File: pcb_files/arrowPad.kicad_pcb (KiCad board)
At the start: 2 copper layers, 43 parts, among them J1 AudioJack3_Ground, J2 AudioJack3_Ground, K1 KEYSW, K10 KEYSW, K11 KEYSW, K12 KEYSW, K13 KEYSW, K14 KEYSW, K15 KEYSW, K16 KEYSW, K2 KEYSW, K3 KEYSW, K4 KEYSW, K5 KEYSW, K6 KEYSW, K7 KEYSW, K8 KEYSW, K9 KEYSW, U1 ProMicro, U2 NRF24L01_Breakout, U3 ADG417BN, U4 AMS1117-3.3, U5 ADG417BN, U6 ADG417BN

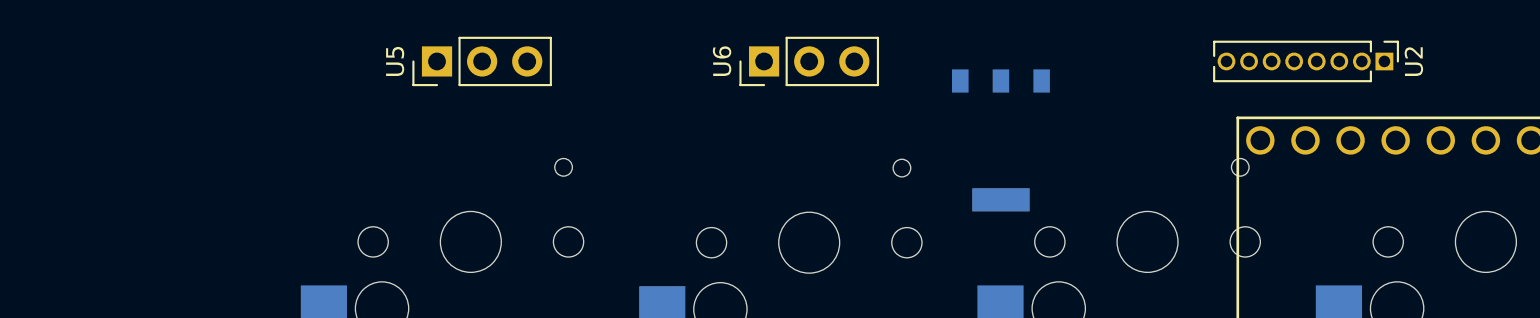
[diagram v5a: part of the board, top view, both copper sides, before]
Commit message: flipped the position of nrf24l01
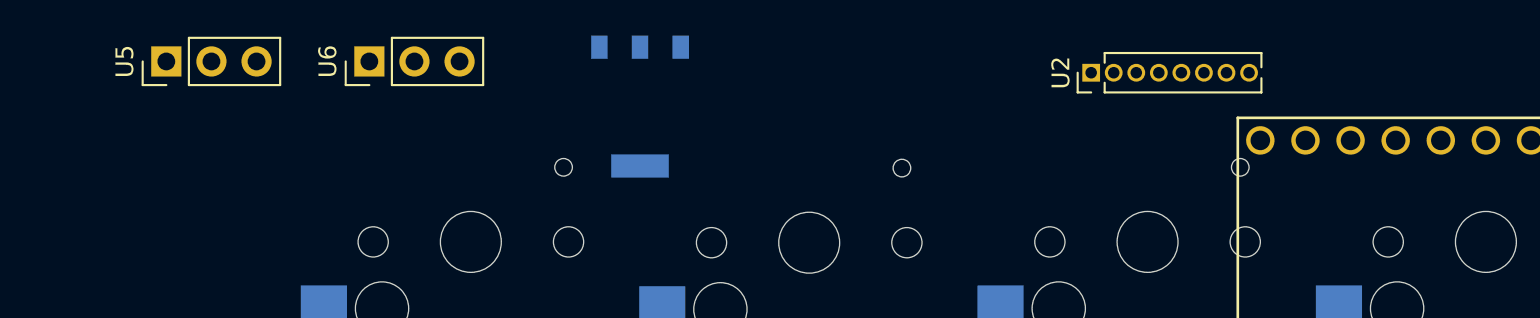
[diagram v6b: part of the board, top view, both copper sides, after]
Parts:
- moved U6 22.2 mm to (125.1, 54.6)
- moved U4 20.4 mm to (140.3, 57.1)
- moved U2 16.5 mm to (165.7, 55.2), turned to 90 degrees
- moved U5 15.2 mm to (113.7, 54.6)
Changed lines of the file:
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@@
   )
   (module keyboard_parts:nrf24l01header (layer F.Cu)
-    (at 182.245 54.61 270)
+    (at 165.735 55.245 90)
     (descr "Through hole straight pin header, 1x08, 1.27mm pitch, single row")
     (tags "Through hole pin header THT 1x08 1.27mm single row")
-    (fp_text reference U2 (at 0 -1.695 270) (layer F.SilkS)
-      (effects (font (size 1 1) (thickness 0.15)))
-    )
-    (fp_text value NRF24L01_Breakout (at 0 10.585 270) (layer F.Fab)
-      (effects (font (size 1 1) (thickness 0.15)))
-    )
+    (fp_text reference U2 (at 0 -1.695 90) (layer F.SilkS)
+      (effects (font (size 1 1) (thickness 0.15)))
+    )
+    (fp_text value NRF24L01_Breakout (at 0 10.585 90) (layer F.Fab)
+      (effects (font (size 1 1) (thickness 0.15)))
+    )
+    (fp_text user %R (at 0 4.445 -180) (layer F.Fab)
+      (effects (font (size 1 1) (thickness 0.15)))
+    )
+    (fp_line (start 1.55 -1.15) (end -1.55 -1.15) (layer F.CrtYd) (width 0.05))
+    (fp_line (start 1.55 10.05) (end 1.55 -1.15) (layer F.CrtYd) (width 0.05))
+    (fp_line (start -1.55 10.05) (end 1.55 10.05) (layer F.CrtYd) (width 0.05))
+    (fp_line (start -1.55 -1.15) (end -1.55 10.05) (layer F.CrtYd) (width 0.05))
+    (fp_line (start -1.11 -0.76) (end 0 -0.76) (layer F.SilkS) (width 0.12))
+    (fp_line (start -1.11 0) (end -1.11 -0.76) (layer F.SilkS) (width 0.12))
+    (fp_line (start 0.563471 0.76) (end 1.11 0.76) (layer F.SilkS) (width 0.12))
+    (fp_line (start -1.11 0.76) (end -0.563471 0.76) (layer F.SilkS) (width 0.12))
+    (fp_line (start 1.11 0.76) (end 1.11 9.585) (layer F.SilkS) (width 0.12))
+    (fp_line (start -1.11 0.76) (end -1.11 9.585) (layer F.SilkS) (width 0.12))
+    (fp_line (start 0.30753 9.585) (end 1.11 9.585) (layer F.SilkS) (width 0.12))
+    (fp_line (start -1.11 9.585) (end -0.30753 9.585) (layer F.SilkS) (width 0.12))
+    (fp_line (start -1.05 -0.11) (end -0.525 -0.635) (layer F.Fab) (width 0.1))
+    (fp_line (start -1.05 9.525) (end -1.05 -0.11) (layer F.Fab) (width 0.1))
+    (fp_line (start 1.05 9.525) (end -1.05 9.525) (layer F.Fab) (width 0.1))
+    (fp_line (start 1.05 -0.635) (end 1.05 9.525) (layer F.Fab) (width 0.1))
     (fp_line (start -0.525 -0.635) (end 1.05 -0.635) (layer F.Fab) (width 0.1))
-    (fp_line (start 1.05 -0.635) (end 1.05 9.525) (layer F.Fab) (width 0.1))
-    (fp_line (start 1.05 9.525) (end -1.05 9.525) (layer F.Fab) (width 0.1))
-    (fp_line (start -1.05 9.525) (end -1.05 -0.11) (layer F.Fab) (width 0.1))
-    (fp_line (start -1.05 -0.11) (end -0.525 -0.635) (layer F.Fab) (width 0.1))
-    (fp_line (start -1.11 9.585) (end -0.30753 9.585) (layer F.SilkS) (width 0.12))
-    (fp_line (start 0.30753 9.585) (end 1.11 9.585) (layer F.SilkS) (width 0.12))
-    (fp_line (start -1.11 0.76) (end -1.11 9.585) (layer F.SilkS) (width 0.12))
-    (fp_line (start 1.11 0.76) (end 1.11 9.585) (layer F.SilkS) (width 0.12))
-    (fp_line (start -1.11 0.76) (end -0.563471 0.76) (layer F.SilkS) (width 0.12))
-    (fp_line (start 0.563471 0.76) (end 1.11 0.76) (layer F.SilkS) (width 0.12))
-    (fp_line (start -1.11 0) (end -1.11 -0.76) (layer F.SilkS) (width 0.12))
-    (fp_line (start -1.11 -0.76) (end 0 -0.76) (layer F.SilkS) (width 0.12))
-    (fp_line (start -1.55 -1.15) (end -1.55 10.05) (layer F.CrtYd) (width 0.05))
-    (fp_line (start -1.55 10.05) (end 1.55 10.05) (layer F.CrtYd) (width 0.05))
-    (fp_line (start 1.55 10.05) (end 1.55 -1.15) (layer F.CrtYd) (width 0.05))
-    (fp_line (start 1.55 -1.15) (end -1.55 -1.15) (layer F.CrtYd) (width 0.05))
-    (fp_text user %R (at 0 4.445) (layer F.Fab)
-      (effects (font (size 1 1) (thickness 0.15)))
-    )
-    (pad 2 thru_hole rect (at 0 0 270) (size 1 1) (drill 0.65) (layers *.Cu *.Mask)
+    (pad 8 thru_hole oval (at 0 8.89 90) (size 1 1) (drill 0.65) (layers *.Cu *.Mask)
+      (net 26 "Net-(U2-Pad8)"))
+    (pad 7 thru_hole oval (at 0 7.62 90) (size 1 1) (drill 0.65) (layers *.Cu *.Mask)
+      (net 21 "Net-(U1-Pad15)"))
+    (pad 6 thru_hole oval (at 0 6.35 90) (size 1 1) (drill 0.65) (layers *.Cu *.Mask)
+      (net 20 "Net-(U1-Pad14)"))
+    (pad 5 thru_hole oval (at 0 5.08 90) (size 1 1) (drill 0.65) (layers *.Cu *.Mask)
+      (net 22 "Net-(U1-Pad16)"))
+    (pad 4 thru_hole oval (at 0 3.81 90) (size 1 1) (drill 0.65) (layers *.Cu *.Mask)
+      (net 23 "Net-(U1-Pad17)"))
+    (pad 3 thru_hole oval (at 0 2.54 90) (size 1 1) (drill 0.65) (layers *.Cu *.Mask)
+      (net 24 "Net-(U1-Pad18)"))
+    (pad 1 thru_hole oval (at 0 1.27 90) (size 1 1) (drill 0.65) (layers *.Cu *.Mask)
+      (net 2 /GND1))
+    (pad 2 thru_hole rect (at 0 0 90) (size 1 1) (drill 0.65) (layers *.Cu *.Mask)
       (net 32 "Net-(U2-Pad2)"))
-    (pad 1 thru_hole oval (at 0 1.27 270) (size 1 1) (drill 0.65) (layers *.Cu *.Mask)
-      (net 2 /GND1))
-    (pad 3 thru_hole oval (at 0 2.54 270) (size 1 1) (drill 0.65) (layers *.Cu *.Mask)
-      (net 24 "Net-(U1-Pad18)"))
-    (pad 4 thru_hole oval (at 0 3.81 270) (size 1 1) (drill 0.65) (layers *.Cu *.Mask)
-      (net 23 "Net-(U1-Pad17)"))
-    (pad 5 thru_hole oval (at 0 5.08 270) (size 1 1) (drill 0.65) (layers *.Cu *.Mask)
-      (net 22 "Net-(U1-Pad16)"))
-    (pad 6 thru_hole oval (at 0 6.35 270) (size 1 1) (drill 0.65) (layers *.Cu *.Mask)
-      (net 20 "Net-(U1-Pad14)"))
-    (pad 7 thru_hole oval (at 0 7.62 270) (size 1 1) (drill 0.65) (layers *.Cu *.Mask)
-      (net 21 "Net-(U1-Pad15)"))
-    (pad 8 thru_hole oval (at 0 8.89 270) (size 1 1) (drill 0.65) (layers *.Cu *.Mask)
-      (net 26 "Net-(U2-Pad8)"))
     (model ${KISYS3DMOD}/Connector_PinHeader_1.27mm.3dshapes/PinHeader_1x08_P1.27mm_Vertical.wrl
       (at (xyz 0 0 0))
@@
   )
   (module promicro:AMS1117flipped (layer F.Cu)
-    (at 160.655 59.055 180)
+    (at 140.335 57.15 180)
     (attr smd)
     (fp_text reference U4 (at -1.15205 -5.14412 180) (layer B.SilkS)
@@
   )
   (module Connector_PinHeader_2.54mm:PinHeader_1x03_P2.54mm_Vertical (layer F.Cu)
-    (at 128.905 54.61 90)
+    (at 113.665 54.61 90)
     (descr "Through hole straight pin header, 1x03, 2.54mm pitch, single row")
     (tags "Through hole pin header THT 1x03 2.54mm single row")
@@
   )
   (module Connector_PinHeader_2.54mm:PinHeader_1x03_P2.54mm_Vertical (layer F.Cu)
-    (at 147.32 54.61 90)
+    (at 125.095 54.61 90)
     (descr "Through hole straight pin header, 1x03, 2.54mm pitch, single row")
     (tags "Through hole pin header THT 1x03 2.54mm single row")

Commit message: start tracing
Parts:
- J1, J2: footprint foots:CUI_SJ1-3514-SMT[PAD1,2,34] -> foots:CUI_SJ1-3514-SMT[PAD1,2,34]Backside
- moved U5 65.4 mm to (114.3, 120.0), turned to 180 degrees
- moved R1 32.5 mm to (200.0, 112.4), turned to 180 degrees
- moved R2 26.8 mm to (115.6, 107.3), turned to 0 degrees
- moved U3 5.68 mm to (203.8, 123.8)
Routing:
- net /RAW1: track 0.00 -> 205.3 mm
- net /VCC1: track 0.00 -> 124.3 mm, vias 0 -> 2
- net Net-(R1-Pad2): track 0.00 -> 123.2 mm
- net /GND1: track 0.00 -> 107.8 mm, vias 0 -> 1
- net /Row2: track 0.00 -> 62.8 mm
- net /Row3: track 0.00 -> 61.8 mm
- net /Row4: track 0.00 -> 59.9 mm
- net Net-(J1-Pad1): track 0.00 -> 49.9 mm
- net /Row1: track 0.00 -> 36.8 mm
- net Net-(U2-Pad2): track 0.00 -> 26.1 mm
- net Net-(J1-Pad2): track 0.00 -> 23.3 mm
- net Net-(U1-Pad18): track 0.00 -> 23.1 mm
- net Net-(U1-Pad17): track 0.00 -> 18.9 mm
- net Net-(D4-Pad2): track 0.00 -> 17.6 mm
- net Net-(U1-Pad16): track 0.00 -> 14.7 mm
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
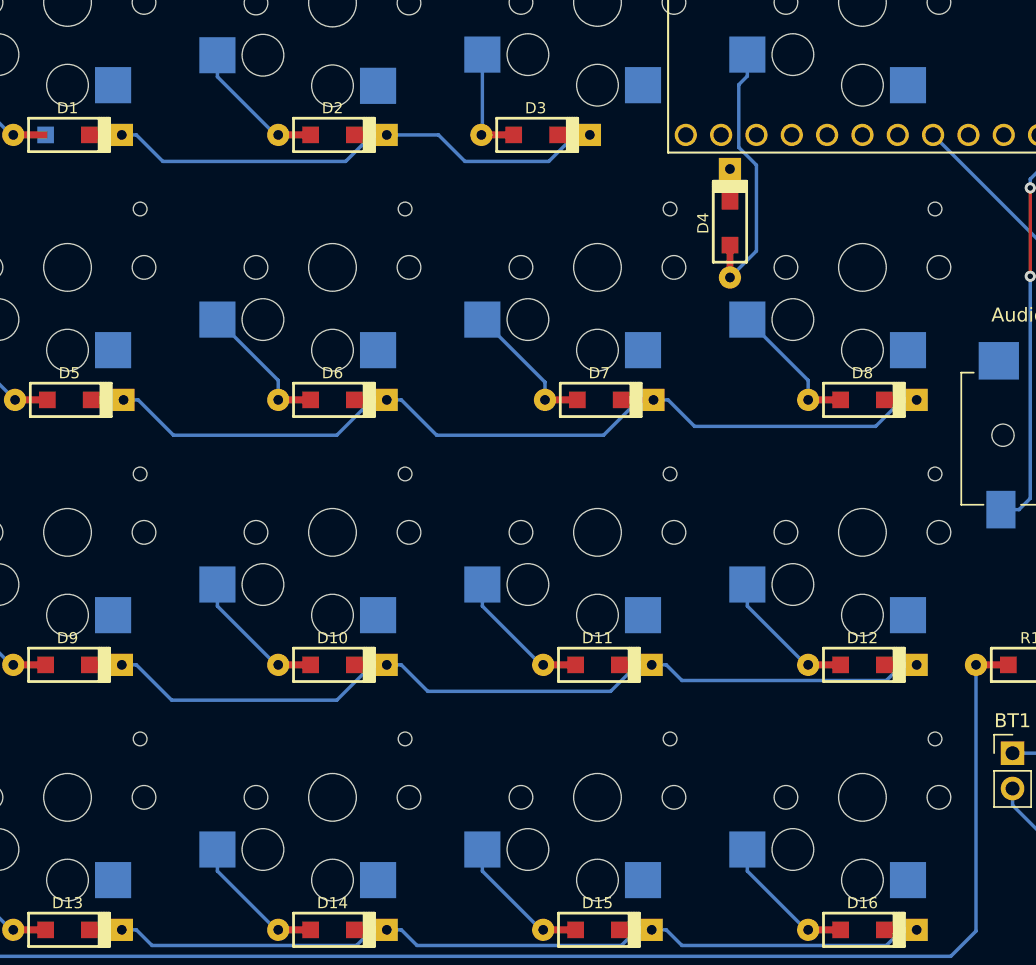
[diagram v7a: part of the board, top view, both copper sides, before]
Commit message: added traces to key matrix
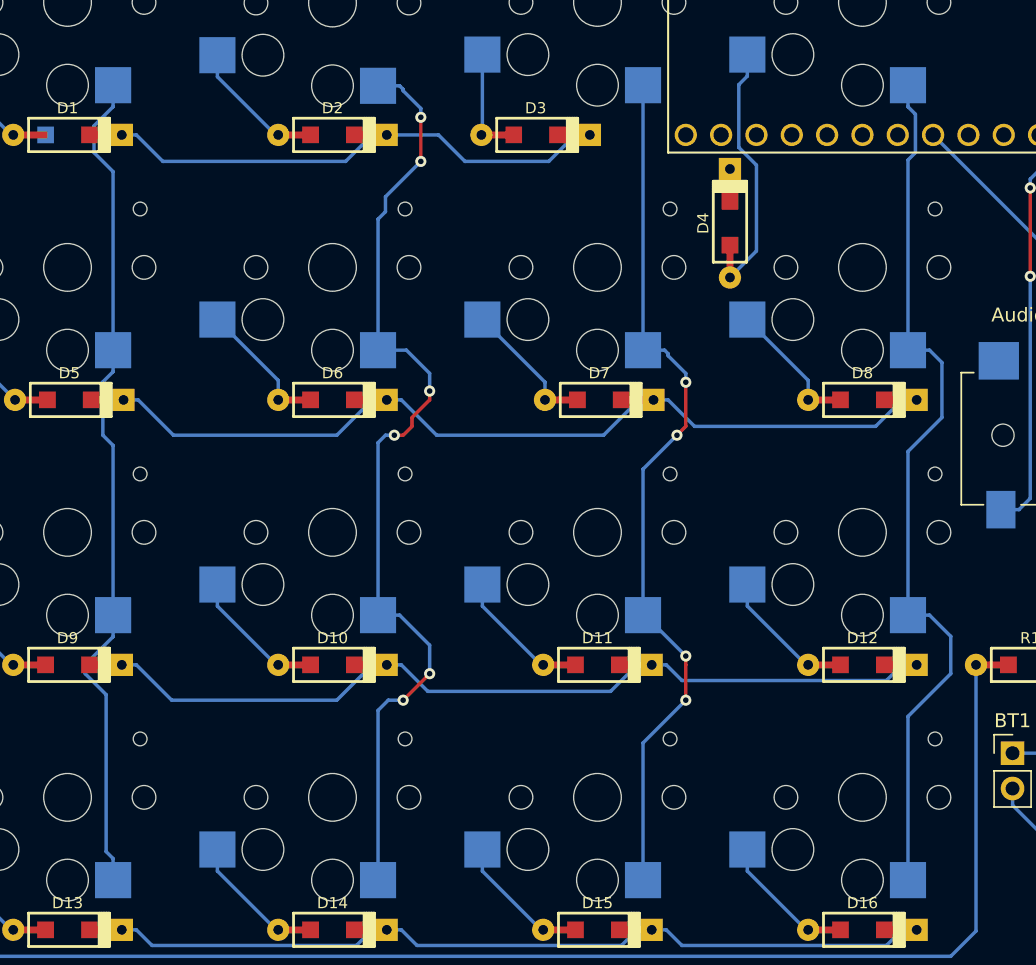
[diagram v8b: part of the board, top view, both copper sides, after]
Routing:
- net /Col2: track 0.00 -> 70.2 mm, vias 0 -> 6
- net /Col4: track 0.00 -> 64.0 mm
- net /Col3: track 0.00 -> 63.2 mm, vias 0 -> 4
- net /Col1: track 0.00 -> 60.6 mm
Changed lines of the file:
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@@
     (thickness 1.6)
     (drawings 0)
-    (tracks 204)
+    (tracks 290)
     (zones 0)
     (modules 43)
@@
   (segment (start 122.535 108.17) (end 126.76 112.395) (width 0.25) (layer B.Cu) (net 14))
   (segment (start 122.535 106.62) (end 122.535 108.17) (width 0.25) (layer B.Cu) (net 14))
+  (segment (start 133.584999 125.819999) (end 133.584999 114.534999) (width 0.25) (layer B.Cu) (net 15))
+  (segment (start 134.085 126.32) (end 133.584999 125.819999) (width 0.25) (layer B.Cu) (net 15))
+  (segment (start 134.085 127.87) (end 134.085 126.32) (width 0.25) (layer B.Cu) (net 15))
+  (segment (start 133.584999 114.534999) (end 132.08 113.03) (width 0.25) (layer B.Cu) (net 15))
+  (segment (start 132.08 112.375) (end 134.085 110.37) (width 0.25) (layer B.Cu) (net 15))
+  (segment (start 134.085 110.37) (end 134.085 108.82) (width 0.25) (layer B.Cu) (net 15))
+  (segment (start 132.08 113.03) (end 132.08 112.375) (width 0.25) (layer B.Cu) (net 15))
+  (segment (start 134.085 108.82) (end 134.085 96.62) (width 0.25) (layer B.Cu) (net 15))
+  (segment (start 134.085 91.32) (end 134.085 89.77) (width 0.25) (layer B.Cu) (net 15))
+  (segment (start 133.35 92.055) (end 134.085 91.32) (width 0.25) (layer B.Cu) (net 15))
+  (segment (start 133.35 95.885) (end 133.35 92.055) (width 0.25) (layer B.Cu) (net 15))
+  (segment (start 134.085 96.62) (end 133.35 95.885) (width 0.25) (layer B.Cu) (net 15))
+  (segment (start 134.085 89.77) (end 134.085 76.935) (width 0.25) (layer B.Cu) (net 15))
+  (segment (start 134.085 76.935) (end 132.715 75.565) (width 0.25) (layer B.Cu) (net 15))
+  (segment (start 134.085 72.27) (end 134.085 70.72) (width 0.25) (layer B.Cu) (net 15))
+  (segment (start 132.715 73.64) (end 134.085 72.27) (width 0.25) (layer B.Cu) (net 15))
+  (segment (start 132.715 75.565) (end 132.715 73.64) (width 0.25) (layer B.Cu) (net 15))
+  (segment (start 153.135 127.87) (end 153.135 115.67) (width 0.25) (layer B.Cu) (net 16))
+  (via (at 154.94 114.935) (size 0.8) (drill 0.4) (layers F.Cu B.Cu) (net 16))
+  (segment (start 153.87 114.935) (end 154.94 114.935) (width 0.25) (layer B.Cu) (net 16))
+  (segment (start 153.135 115.67) (end 153.87 114.935) (width 0.25) (layer B.Cu) (net 16))
+  (segment (start 154.94 114.935) (end 156.845 113.03) (width 0.25) (layer F.Cu) (net 16))
+  (via (at 156.845 113.03) (size 0.8) (drill 0.4) (layers F.Cu B.Cu) (net 16))
+  (segment (start 154.685 108.82) (end 153.135 108.82) (width 0.25) (layer B.Cu) (net 16))
+  (segment (start 156.845 110.98) (end 154.685 108.82) (width 0.25) (layer B.Cu) (net 16))
+  (segment (start 156.845 113.03) (end 156.845 110.98) (width 0.25) (layer B.Cu) (net 16))
+  (segment (start 153.135 108.82) (end 153.135 96.42) (width 0.25) (layer B.Cu) (net 16))
+  (segment (start 155.575 95.25) (end 155.575 94.615) (width 0.25) (layer F.Cu) (net 16))
+  (via (at 156.845 92.71) (size 0.8) (drill 0.4) (layers F.Cu B.Cu) (net 16))
+  (segment (start 156.845 93.345) (end 156.845 92.71) (width 0.25) (layer F.Cu) (net 16))
+  (segment (start 155.575 94.615) (end 156.845 93.345) (width 0.25) (layer F.Cu) (net 16))
+  (segment (start 156.845 92.71) (end 156.845 91.44) (width 0.25) (layer B.Cu) (net 16))
+  (segment (start 155.175 89.77) (end 153.135 89.77) (width 0.25) (layer B.Cu) (net 16))
+  (segment (start 156.845 91.44) (end 155.175 89.77) (width 0.25) (layer B.Cu) (net 16))
+  (segment (start 153.135 96.42) (end 153.67 95.885) (width 0.25) (layer B.Cu) (net 16))
+  (via (at 154.305 95.885) (size 0.8) (drill 0.4) (layers F.Cu B.Cu) (net 16))
+  (segment (start 153.67 95.885) (end 154.305 95.885) (width 0.25) (layer B.Cu) (net 16))
+  (segment (start 154.305 95.885) (end 154.94 95.885) (width 0.25) (layer F.Cu) (net 16))
+  (segment (start 154.94 95.885) (end 155.575 95.25) (width 0.25) (layer F.Cu) (net 16))
+  (segment (start 153.135 80.350954) (end 153.67 79.815954) (width 0.25) (layer B.Cu) (net 16))
+  (segment (start 153.135 89.77) (end 153.135 80.350954) (width 0.25) (layer B.Cu) (net 16))
+  (segment (start 153.67 79.815954) (end 153.67 78.74) (width 0.25) (layer B.Cu) (net 16))
+  (via (at 156.21 76.2) (size 0.8) (drill 0.4) (layers F.Cu B.Cu) (net 16))
+  (segment (start 153.67 78.74) (end 156.21 76.2) (width 0.25) (layer B.Cu) (net 16))
+  (segment (start 156.21 76.2) (end 156.21 73.025) (width 0.25) (layer F.Cu) (net 16))
+  (via (at 156.21 73.025) (size 0.8) (drill 0.4) (layers F.Cu B.Cu) (net 16))
+  (segment (start 156.21 73.025) (end 156.21 72.39) (width 0.25) (layer B.Cu) (net 16))
+  (segment (start 156.21 72.39) (end 154.94 71.12) (width 0.25) (layer B.Cu) (net 16))
+  (segment (start 154.685 70.764) (end 153.135 70.764) (width 0.25) (layer B.Cu) (net 16))
+  (segment (start 154.94 71.019) (end 154.685 70.764) (width 0.25) (layer B.Cu) (net 16))
+  (segment (start 154.94 71.12) (end 154.94 71.019) (width 0.25) (layer B.Cu) (net 16))
+  (segment (start 172.185 127.87) (end 172.185 118.01) (width 0.25) (layer B.Cu) (net 17))
+  (via (at 175.26 114.935) (size 0.8) (drill 0.4) (layers F.Cu B.Cu) (net 17))
+  (segment (start 172.185 118.01) (end 175.26 114.935) (width 0.25) (layer B.Cu) (net 17))
+  (segment (start 175.26 114.935) (end 175.26 112.395) (width 0.25) (layer F.Cu) (net 17))
+  (via (at 175.26 111.76) (size 0.8) (drill 0.4) (layers F.Cu B.Cu) (net 17))
+  (segment (start 175.26 112.395) (end 175.26 111.76) (width 0.25) (layer F.Cu) (net 17))
+  (segment (start 172.32 108.82) (end 172.185 108.82) (width 0.25) (layer B.Cu) (net 17))
+  (segment (start 175.26 111.76) (end 172.32 108.82) (width 0.25) (layer B.Cu) (net 17))
+  (segment (start 172.185 108.82) (end 172.185 98.325) (width 0.25) (layer B.Cu) (net 17))
+  (via (at 174.625 95.885) (size 0.8) (drill 0.4) (layers F.Cu B.Cu) (net 17))
+  (segment (start 172.185 98.325) (end 174.625 95.885) (width 0.25) (layer B.Cu) (net 17))
+  (segment (start 174.625 95.885) (end 175.26 95.25) (width 0.25) (layer F.Cu) (net 17))
+  (via (at 175.26 92.075) (size 0.8) (drill 0.4) (layers F.Cu B.Cu) (net 17))
+  (segment (start 175.26 95.25) (end 175.26 92.075) (width 0.25) (layer F.Cu) (net 17))
+  (segment (start 175.26 92.075) (end 175.26 91.44) (width 0.25) (layer B.Cu) (net 17))
+  (segment (start 175.26 91.44) (end 173.99 90.17) (width 0.25) (layer B.Cu) (net 17))
+  (segment (start 173.735 89.77) (end 172.185 89.77) (width 0.25) (layer B.Cu) (net 17))
+  (segment (start 173.99 90.025) (end 173.735 89.77) (width 0.25) (layer B.Cu) (net 17))
+  (segment (start 173.99 90.17) (end 173.99 90.025) (width 0.25) (layer B.Cu) (net 17))
+  (segment (start 172.185 89.77) (end 172.185 70.72) (width 0.25) (layer B.Cu) (net 17))
   (segment (start 174.769999 57.929999) (end 176.674999 57.929999) (width 0.25) (layer B.Cu) (net 20))
   (segment (start 177.000001 58.255001) (end 177.8 59.055) (width 0.25) (layer B.Cu) (net 20))
@@
   (segment (start 200.025 77.47) (end 201.295 76.2) (width 0.25) (layer B.Cu) (net 40))
   (segment (start 200.025 78.105) (end 200.025 77.47) (width 0.25) (layer B.Cu) (net 40))
+  (segment (start 191.235 127.87) (end 191.235 116.105) (width 0.25) (layer B.Cu) (net 41))
+  (segment (start 191.235 116.105) (end 194.31 113.03) (width 0.25) (layer B.Cu) (net 41))
+  (segment (start 194.31 110.345) (end 192.785 108.82) (width 0.25) (layer B.Cu) (net 41))
+  (segment (start 192.785 108.82) (end 191.235 108.82) (width 0.25) (layer B.Cu) (net 41))
+  (segment (start 194.31 113.03) (end 194.31 110.345) (width 0.25) (layer B.Cu) (net 41))
+  (segment (start 191.235 108.82) (end 191.235 97.055) (width 0.25) (layer B.Cu) (net 41))
+  (segment (start 191.235 97.055) (end 193.675 94.615) (width 0.25) (layer B.Cu) (net 41))
+  (segment (start 192.785 89.77) (end 191.235 89.77) (width 0.25) (layer B.Cu) (net 41))
+  (segment (start 193.675 90.66) (end 192.785 89.77) (width 0.25) (layer B.Cu) (net 41))
+  (segment (start 193.675 94.615) (end 193.675 90.66) (width 0.25) (layer B.Cu) (net 41))
+  (segment (start 191.235 89.77) (end 191.235 76.1) (width 0.25) (layer B.Cu) (net 41))
+  (segment (start 191.235 72.27) (end 191.235 70.72) (width 0.25) (layer B.Cu) (net 41))
+  (segment (start 191.77 72.805) (end 191.235 72.27) (width 0.25) (layer B.Cu) (net 41))
+  (segment (start 191.77 75.565) (end 191.77 72.805) (width 0.25) (layer B.Cu) (net 41))
+  (segment (start 191.235 76.1) (end 191.77 75.565) (width 0.25) (layer B.Cu) (net 41))
   (segment (start 119.47 112.305) (end 114.3 117.475) (width 0.25) (layer B.Cu) (net 45))
   (segment (start 119.47 107.315) (end 119.47 112.305) (width 0.25) (layer B.Cu) (net 45))
